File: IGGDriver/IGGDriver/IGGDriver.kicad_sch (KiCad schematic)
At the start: 88 parts, among them J1 Conn_01x02, J2 Conn_01x05, J3 Conn_01x04, J4 Conn_01x02, J5 Conn_ARM_SWD_TagConnect_TC203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, J6 USB_C_Receptacle_USB2.0, SW1 SW_Push, SW2 SW_Push, U1 AMS1117-5.0, U10 74AHCT595, U11 74AHCT595, U12 W25Q128JVS, U14 RP2040, U15 74HC14, U2 AMS1117-3.3, U3 MT3608, U4 74AHCT595, U5 74AHCT595, U6 74AHCT595, U7 74AHCT595, U8 74AHCT595, U9 74AHCT595, Y1 12M

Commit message: combined the pcbs, now to relayout. :(
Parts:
- added BT1, BT2, BT3: Battery, Battery:BatteryHolder_MPD_BH-18650-PC2, symbol Device:Battery
- U13: footprint IGG1:IGG1-Anode -> IGG1:IGG1-All; symbol IGG1:IGG1-64 -> IGG1:IGG1-64-All
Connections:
- net AO1: now also U13.65 (A1); no longer U13.1
- net AO10: now also U13.74 (A10); no longer U13.10
- net AO11: now also U13.75 (A11); no longer U13.11
- net AO12: now also U13.76 (A12); no longer U13.12
- net AO13: now also U13.77 (A13); no longer U13.13
- net AO14: now also U13.78 (A14); no longer U13.14
- net AO15: now also U13.79 (A15); no longer U13.15
- net AO16: now also U13.80 (A16); no longer U13.16
- net AO17: now also U13.81 (A17); no longer U13.17
- net AO18: now also U13.82 (A18); no longer U13.18
- net AO19: now also U13.83 (A19); no longer U13.19
- net AO2: now also U13.66 (A2); no longer U13.2
- net AO20: now also U13.84 (A20); no longer U13.20
- net AO21: now also U13.85 (A21); no longer U13.21
- net AO22: now also U13.86 (A22); no longer U13.22
- net AO23: now also U13.87 (A23); no longer U13.23
- net AO24: now also U13.88 (A24); no longer U13.24
- net AO25: now also U13.89 (A25); no longer U13.25
- net AO26: now also U13.90 (A26); no longer U13.26
- net AO27: now also U13.91 (A27); no longer U13.27
- net AO28: now also U13.92 (A28); no longer U13.28
- net AO29: now also U13.93 (A29); no longer U13.29
- net AO3: now also U13.67 (A3); no longer U13.3
- net AO30: now also U13.94 (A30); no longer U13.30
- net AO31: now also U13.95 (A31); no longer U13.31
- net AO32: now also U13.96 (A32); no longer U13.32
- net AO33: now also U13.97 (A33); no longer U13.33
- net AO34: now also U13.98 (A34); no longer U13.34
- net AO35: now also U13.99 (A35); no longer U13.35
- net AO36: now also U13.100 (A36); no longer U13.36
- net AO37: now also U13.101 (A37); no longer U13.37
- net AO38: now also U13.102 (A38); no longer U13.38
- net AO39: now also U13.103 (A39); no longer U13.39
- net AO4: now also U13.68 (A4); no longer U13.4
- net AO40: now also U13.104 (A40); no longer U13.40
- net AO41: now also U13.105 (A41); no longer U13.41
- net AO42: now also U13.106 (A42); no longer U13.42
- net AO43: now also U13.107 (A43); no longer U13.43
- net AO44: now also U13.108 (A44); no longer U13.44
- net AO45: now also U13.109 (A45); no longer U13.45
- net AO46: now also U13.110 (A46); no longer U13.46
- net AO47: now also U13.111 (A47); no longer U13.47
- net AO48: now also U13.112 (A48); no longer U13.48
- net AO49: now also U13.113 (A49); no longer U13.49
- net AO5: now also U13.69 (A5); no longer U13.5
- net AO50: now also U13.114 (A50); no longer U13.50
- net AO51: now also U13.115 (A51); no longer U13.51
- net AO52: now also U13.116 (A52); no longer U13.52
- net AO53: now also U13.117 (A53); no longer U13.53
- net AO54: now also U13.118 (A54); no longer U13.54
- net AO55: now also U13.119 (A55); no longer U13.55
- net AO56: now also U13.120 (A56); no longer U13.56
- net AO57: now also U13.121 (A57); no longer U13.57
- net AO58: now also U13.122 (A58); no longer U13.58
- net AO59: now also U13.123 (A59); no longer U13.59
- net AO6: now also U13.70 (A6); no longer U13.6
- net AO60: now also U13.124 (A60); no longer U13.60
- net AO61: now also U13.125 (A61); no longer U13.61
- net AO62: now also U13.126 (A62); no longer U13.62
- net AO63: now also U13.127 (A63); no longer U13.63
- net AO64: now also U13.128 (A64); no longer U13.64
- net AO7: now also U13.71 (A7); no longer U13.7
- net AO8: now also U13.72 (A8); no longer U13.8
- net AO9: now also U13.73 (A9); no longer U13.9

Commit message: almost done
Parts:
- removed BT1, BT2, BT3: Battery, Battery:BatteryHolder_MPD_BH-18650-PC2, symbol Device:Battery
- removed C15, C6: 22u, Capacitor_SMD:C_1206_3216Metric, symbol Device:C
- removed D7: D, Diode_SMD:D_SMA, symbol Device:D
- removed L1: 22uH, Inductor_SMD:L_Chilisin_BMRF00101040, symbol Device:L
- removed R5, R7: 10K, Resistor_SMD:R_0603_1608Metric, symbol Device:R
- removed R6: 200K, Resistor_SMD:R_0603_1608Metric, symbol Device:R
- removed U3: MT3608, Package_TO_SOT_SMD:SOT-23-6, symbol Regulator_Switching:MT3608
- added J8: Micro_SD_Card_Det_Hirose_DM3AT, Connector_Card:microSD_HC_Hirose_DM3D-SF, symbol Connector:Micro_SD_Card_Det_Hirose_DM3AT
- added U3: FSUSB42MUX, Package_SO:MSOP-10_3x3mm_P0.5mm, symbol Interface_USB:FSUSB42MUX
- J6: footprint Connector_USB:USB_C_Receptacle_HRO_TYPE-C-31-M-12 -> Connector_USB:USB_C_Receptacle_GCT_USB4115-03-C
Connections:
- removed net USB_D+: J6.A6 (D+), J6.B6 (D+), R12.2
- removed net USB_D-: J6.A7 (D-), J6.B7 (D-), R13.2
- new net RP_USB_D+: R12.2
- new net RP_USB_D-: R13.2
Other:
- added sheet BatteryManagement (IP2368.kicad_sch)
- added sheet HV_GEN (MAX1771.kicad_sch)
- moved on the sheet: D8, J6, R14, R15

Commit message: progress!
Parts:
- removed D1, D2, D3, D4, D5, D6: SK6812, LED_SMD:LED_SK6812MINI_PLCC4_3.5x3.5mm_P1.75mm, symbol LED:SK6812
- removed J1: Conn_01x02, Connector_JST:JST_XH_B2B-XH-AM_1x02_P2.50mm_Vertical, symbol Connector_Generic:Conn_01x02
- removed J2: Conn_01x05, Connector_JST:JST_XH_B5B-XH-AM_1x05_P2.50mm_Vertical, symbol Connector_Generic:Conn_01x05
- removed J3: Conn_01x04, Connector_JST:JST_XH_B4B-XH-AM_1x04_P2.50mm_Vertical, symbol Connector_Generic:Conn_01x04
- removed JP1, JP2, JP3, JP4, JP5, JP6, JP7: Jumper_2_Open, Jumper:SolderJumper-2_P1.3mm_Open_TrianglePad1.0x1.5mm, symbol Jumper:Jumper_2_Open
- removed unit 1 of U15
- removed unit 2 of U15
- removed unit 3 of U15
- removed unit 4 of U15
- removed U3: FSUSB42MUX, Package_SO:MSOP-10_3x3mm_P0.5mm, symbol Interface_USB:FSUSB42MUX
- added BT3: DNP, Battery:BatteryHolder_Keystone_1060_1x2032, symbol Device:Battery_Cell
- added C106: DNP, Capacitor_THT:C_Rect_L19.0mm_W11.0mm_P15.00mm_MKS4, symbol Device:C_Polarized
- added C6: 1u, Capacitor_SMD:C_0603_1608Metric, symbol Device:C
- added D1, D2, D3, D4, D5: LED, LED_SMD:LED_0603_1608Metric, symbol Device:LED
- added J1, J7: Conn_01x04, Connector_JST:JST_XH_B4B-XH-AM_1x04_P2.50mm_Vertical, symbol Connector_Generic:Conn_01x04
- added J2: ~, USBSolderMux:USBSolderMux, symbol USBSolderMux:USBSolderMux
- added JP10: Jumper_2_Bridged, symbol Jumper:Jumper_2_Bridged
- added JP11: Jumper_2_Open, symbol Jumper:Jumper_2_Open
- added Q131: AO3401A, Package_TO_SOT_SMD:SOT-23, symbol Transistor_FET:AO3401A
- added R281, R291, R293, R294: 4K7, Resistor_SMD:R_0603_1608Metric, symbol Device:R
- added R283, R287, R289, R292, R300: 10K, Resistor_SMD:R_0603_1608Metric, symbol Device:R
- added R288, R295, R296, R297, R298, R299: 1K, Resistor_SMD:R_0603_1608Metric, symbol Device:R
- added R290: 47K, Resistor_SMD:R_0603_1608Metric, symbol Device:R
- added SW3: UP, Button_Switch_SMD:SW_SPST_TL3342, symbol Switch:SW_Push
- added SW4: DOWN, Button_Switch_SMD:SW_SPST_TL3342, symbol Switch:SW_Push
- added SW5: LEFT, Button_Switch_SMD:SW_SPST_TL3342, symbol Switch:SW_Push
- added SW6: RIGHT, Button_Switch_SMD:SW_SPST_TL3342, symbol Switch:SW_Push
- added U19: PCF8523T, Package_SO:SOIC-8_3.9x4.9mm_P1.27mm, symbol Timer_RTC:PCF8523T
- added U20: IIM-42652, Package_LGA:Bosch_LGA-14_3x2.5mm_P0.5mm, symbol Sensor_Motion:IIM-42652
- added Y2: Crystal, Crystal:Crystal_SMD_3215-2Pin_3.2x1.5mm, symbol Device:Crystal
- C17, C19: value 4.7pF -> 20pf; LCSC C1669 -> C1648; LCSC Part C1669 -> C1648
- J8: LCSC (none) -> C719027
- R1: LCSC (none) -> C25819
- SW1: value SW_Push -> BOOT
- SW2: value SW_Push -> RST
- U1: value AMS1117-5.0 -> DNP; LCSC C6187 -> DNP
- U2: LCSC (none) -> C6186
- Y1: footprint Crystal:Crystal_SMD_5032-2Pin_5.0x3.2mm -> Crystal:Crystal_SMD_3225-4Pin_3.2x2.5mm; symbol Device:Crystal -> Device:Crystal_GND24; LCSC C90884 -> C9002; LCSC Part C90884 -> C9002
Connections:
- net A_ADDR_LED is gone; now on net SD_DAT3: U14.35 (GPIO23)
- net K_ADDR_LED is gone; now on net SD_DAT2: U14.34 (GPIO22)
- net +12V: no longer U1.3 (VI)
- net +3V3: now also J8.4 (VDD), C6.1, J1.4 (Pin_4), J7.4 (Pin_4), R288.2, R290.1, R291.1, R292.1, R293.1, R294.1, R300.2, U19.8 (VDD), U20.12 (AP_CS), U20.5 (VDDIO), U20.8 (VDD)
- net +BATT: now also U1.3 (VI), Q131.3 (D), R287.2
- net BAT_DIV: now also U14.39 (GPIO27_ADC1)
- net GND: now also J8.11 (SHIELD), J8.6 (VSS), J8.9 (DET_B), Y1.2, Y1.4, BT3.2 (-), C106.2, C6.2, D1.1 (K), D2.1 (K), D3.1 (K), D4.1 (K), D5.1 (K), J1.1 (Pin_1), J7.1 (Pin_1), R281.1, R283.1, R289.2, U19.4 (VSS), U20.6 (GND), U20.7 (GND)
- net K_CLK: now also U14.18 (GPIO15), R297.1; no longer U14.15 (GPIO12)
- net K_RST: now also U14.17 (GPIO14), R296.1; no longer U14.14 (GPIO11)
- net RP_USB_D+: now also U14.47 (USB_DP), J2.1 (A+); no longer R12.2
- net RP_USB_D-: now also U14.46 (USB_DM), J2.2 (A-); no longer R13.2
- net SR_D2: now also U4.9 (QH')
- net SR_D3: now also U5.9 (QH')
- net SR_D4: now also U6.9 (QH')
- net SR_D5: now also U7.9 (QH')
- net SR_D6: now also U8.9 (QH')
- net SR_D7: now also U9.9 (QH')
- net SR_D8: now also U10.9 (QH')
- net SR_SHCP: now also U14.13 (GPIO10), R295.1; no longer U14.11 (GPIO8)
- net SR_STCP: now also U14.28 (GPIO17); no longer U14.17 (GPIO14)
- net ~SR_MC: now also U14.27 (GPIO16); no longer U14.16 (GPIO13)
- net ~SR_OE: now also U14.29 (GPIO18), R298.1; no longer U14.18 (GPIO15)
- net ~{USB_BOOT}: now also R8.2; no longer R8.1
- net SD_DAT2: now reaches J8.1 (DAT2)
- net SD_DET: now reaches J8.10 (DET_A)
- net SD_DAT3: now reaches J8.2 (DAT3/CD)
- net SD_CMD: now reaches J8.3 (CMD)
- net SD_CMD: now also U14.30 (GPIO19)
- net SD_CLK: now reaches J8.5 (CLK)
- net SD_CLK: now also U14.36 (GPIO24)
- net SD_DAT0: now reaches J8.7 (DAT0)
- net SD_DAT0: now also U14.31 (GPIO20)
- net SD_DAT1: now reaches J8.8 (DAT1)
- net SD_DAT1: now also U14.32 (GPIO21)
- net USB_D+: now reaches R13.1
- net USB_D+: now also J2.5 (C+); no longer U14.46 (USB_DM)
- net at C19.1, U14.21 (XOUT): now also Y1.3; no longer Y1.2
- net at R10.2, U12.1 (~{CS}), U14.56 (QSPI_SS): now also R8.1; no longer R8.2
- net USB_D-: now reaches R12.1
- net USB_D-: now also J2.6 (C-); no longer U14.47 (USB_DP)
- net SCL: now reaches U14.12 (GPIO9)
- net SCL: now also J7.2 (Pin_2), R294.2, U19.6 (SCL), U20.13 (AP_SCL/AP_SCLK)
- net HV_EN: now reaches U14.37 (GPIO25)
- net HV_EN: now also R300.1
- net ANA_SW: now reaches U14.40 (GPIO28_ADC2)
- net ANA_SW: now also R289.1, SW3.2, SW4.2, SW5.2, SW6.2
- net ACCEL_INT: now reaches U14.41 (GPIO29_ADC3)
- net ACCEL_INT: now also U20.4 (INT1/INT)
- net at J6.A6 (D+): now also J6.B6 (D+), R13.2
- net at J6.A7 (D-): now also J6.B7 (D-), R12.2
- new net: D2.2 (A), R296.2
- new net: BT3.1 (+), C106.1, JP10.1 (A), U19.3 (VBAT)
- new net: JP11.1 (A), Q131.2 (S)
- new net: D3.2 (A), R297.2
- new net: R281.2, U20.1 (AP_SDO/AP_AD0)
- new net: D5.2 (A), R299.2
- new net: R288.1, SW3.1
- new net: D1.2 (A), R295.2
- new net: U19.2 (OSCO), Y2.1
- new net: U19.1 (OSCI), Y2.2
- new net: R291.2, SW4.1
- new net: D4.2 (A), R298.2
- new net: R290.2, SW6.1
- new net: R292.2, SW5.1
- new net 5VBuck/EN: JP11.2 (B)
- new net 5V_EN: Q131.1 (G), R283.2, R287.1, U14.14 (GPIO11), U19.7 (~{INT1}/CLKOUT)
- new net BAT_MID: JP10.2 (B)
- new net BMS_USB_D+: J2.4 (B-)
- new net BMS_USB_D-: J2.3 (B+)
- new net LED: J1.2 (Pin_2), R299.1, U14.15 (GPIO12)
- new net RX: J1.3 (Pin_3), U14.16 (GPIO13)
- new net SDA: J7.3 (Pin_3), R293.2, U14.11 (GPIO8), U19.5 (SDA), U20.14 (AP_SDA/AP_SDIO/AP_SDI)
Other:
- added sheet 5VBuck (TPS5430.kicad_sch)
- sheet BatteryManagement ports: added BAT_MID; removed none
- sheet Kathode ports: added INPUT_CLK, RESET; removed none
- note added: "3V 2.245 1.65 0.579"
- note added: "Short jumper to enable RP2040/RTC control"
- moved on the sheet: R12, R13, R8, U1

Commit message: Commit to xfer to other computer
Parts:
- removed C1, C2: 1u, Capacitor_SMD:C_0603_1608Metric, symbol Device:C
- removed J4: Conn_01x02, Connector_JST:JST_XH_B2B-XH-AM_1x02_P2.50mm_Vertical, symbol Connector_Generic:Conn_01x02
- added JP2: Jumper_2_Bridged, symbol Jumper:Jumper_2_Bridged
- added R301: 10K, Resistor_SMD:R_0603_1608Metric, symbol Device:R
- added R302: DNP, Resistor_SMD:R_0603_1608Metric, symbol Device:R
- added SW7: DNP, KAN28:KAN28, symbol Switch:SW_SPST
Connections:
- net +12V is gone; now on net +BATT: R1.1
- net +BATT: now also JP2.1 (A), R301.2, SW7.2 (B)
- net 5VBuck/EN: now also R301.1, R302.2
- net GND: now also R302.1
- net K_CLK: no longer R297.1
- net K_CLK_5V: now also R296.1
- net K_RST: no longer R296.1
- net K_RST_5V: now also R297.1
- new net BatteryManagement/V_OUT: JP2.2 (B), SW7.1 (A)
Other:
- sheet BatteryManagement ports: added none; removed EN
- note added: "Short jumper, swap r301 to R302 to enable RP2040/RTC control"
- note removed: "Short jumper to enable RP2040/RTC control"
- moved on the sheet: D2, D3, JP11, R296, R297

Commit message: Push to other computer to edit footprint
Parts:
- added D139, D140, D6: LED, LED_SMD:LED_0603_1608Metric, symbol Device:LED
- added H5, H6: H, Mounting_Wuerth:Mounting_Wuerth_WA-SMSI-M3_H6mm_9774060360, symbol Mechanical:MountingHole_Pad
- added R303, R304, R305: 1K, Resistor_SMD:R_0603_1608Metric, symbol Device:R
- H1, H2, H3, H4: footprint MountingHole:MountingHole_3.2mm_M3_DIN965_Pad -> Mounting_Wuerth:Mounting_Wuerth_WA-SMSI-M3_H6mm_9774060360
- JP10, JP2: footprint (none) -> Jumper:SolderJumper-2_P1.3mm_Bridged_Pad1.0x1.5mm
- JP11: footprint (none) -> Jumper:SolderJumper-2_P1.3mm_Open_TrianglePad1.0x1.5mm
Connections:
- net +3V3: now also R303.1
- net +5V: now also R304.1
- net +BATT: now also R305.1
- net GND: now also D139.1 (K), D140.1 (K), D6.1 (K), H5.1, H6.1
- net SR_D2: no longer U4.9 (QH')
- net SR_D3: no longer U5.9 (QH')
- net SR_D4: no longer U6.9 (QH')
- net SR_D5: no longer U7.9 (QH')
- net SR_D6: no longer U8.9 (QH')
- net SR_D7: no longer U9.9 (QH')
- net SR_D8: no longer U10.9 (QH')
- new net: D139.2 (A), R304.2
- new net: D140.2 (A), R305.2
- new net: D6.2 (A), R303.2

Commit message: added the footprint for the SMDnuts
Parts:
- H1, H2, H3, H4, H5, H6: footprint Mounting_Wuerth:Mounting_Wuerth_WA-SMSI-M3_H6mm_9774060360 -> SinhooSMDNut:M3x0.5SMDNut; LCSC (none) -> C2915637

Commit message: RTM
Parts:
- C17, C19: LCSC C1648 -> C1648
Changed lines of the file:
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@@
 			)
 		)
-		(property "LCSC" "    C1648"
+		(property "LCSC" "C1648"
 			(at 330.2 295.91 0)
 			(effects
@@
 			)
 		)
-		(property "LCSC" "    C1648"
+		(property "LCSC" "C1648"
 			(at 314.96 295.91 0)
 			(effects

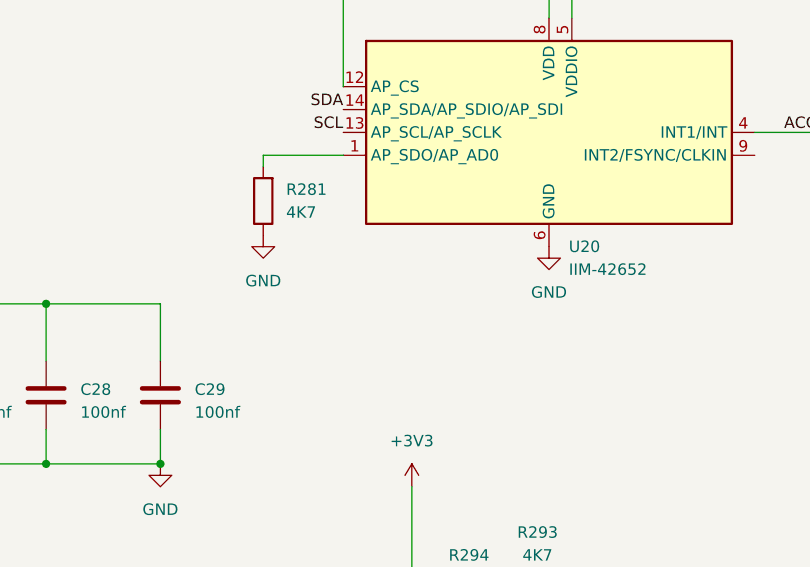
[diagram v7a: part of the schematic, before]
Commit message: Added mechanicDDDDl stuff, case, etc
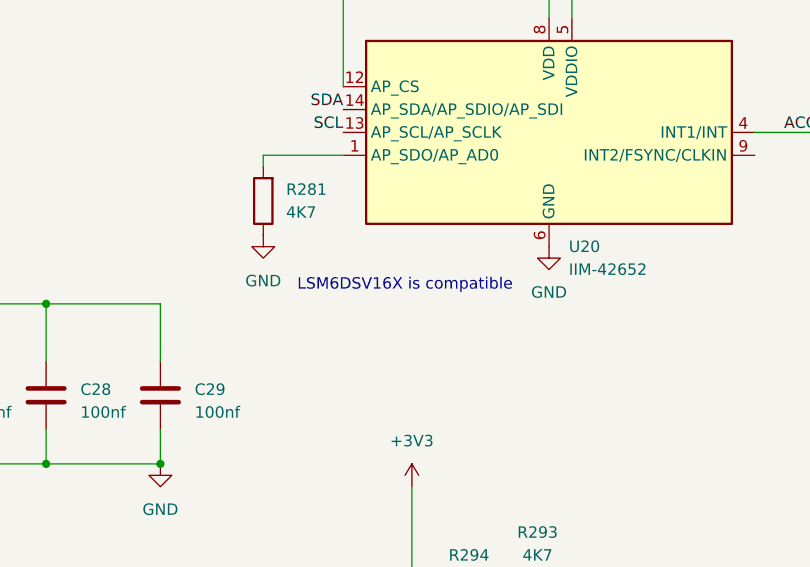
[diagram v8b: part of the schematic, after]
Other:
- note added: "LSM6DSV16X is compatible"
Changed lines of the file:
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@@
+		)
+	)
+	(text "LSM6DSV16X is compatible\n"
+		(exclude_from_sim no)
+		(at 485.648 193.548 0)
+		(effects
+			(font
+				(size 1.27 1.27)
+			)
 		)
 	)
